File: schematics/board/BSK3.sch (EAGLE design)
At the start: 19 parts

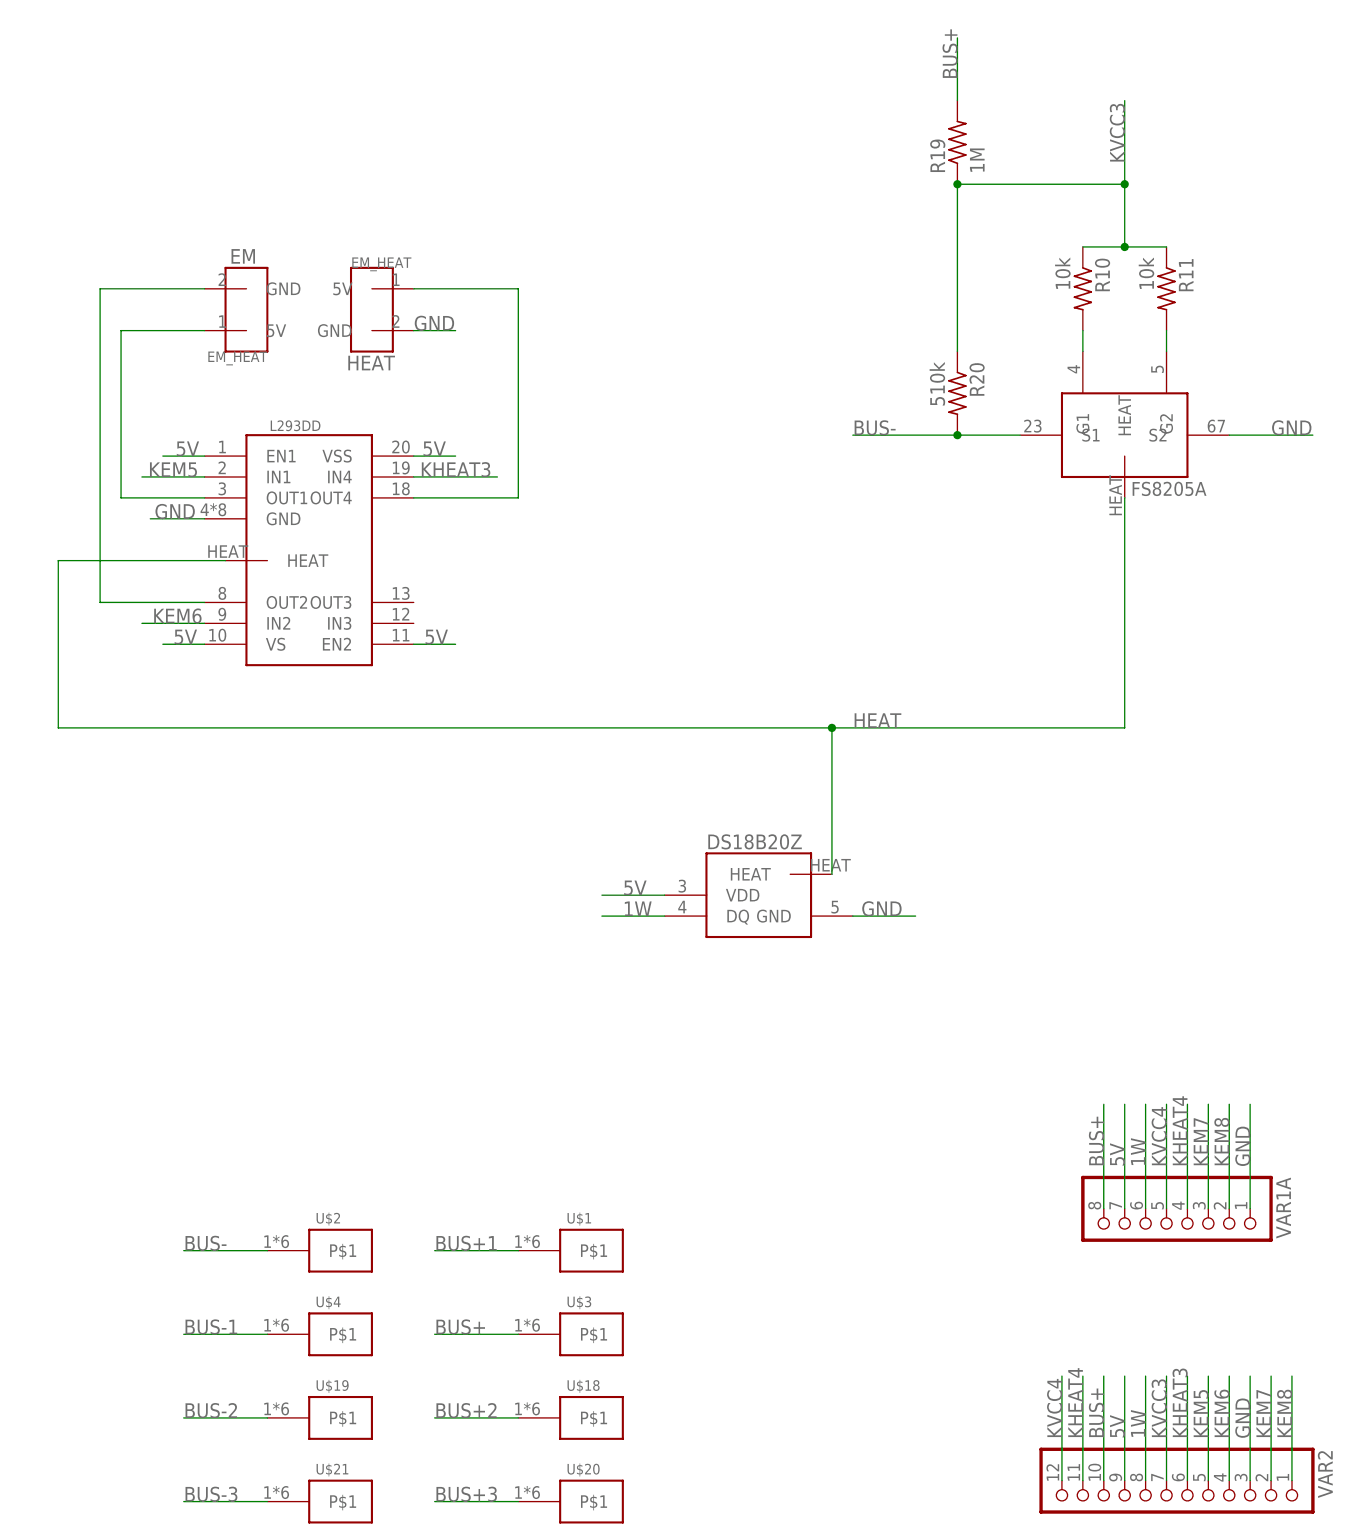
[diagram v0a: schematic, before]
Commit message: Реструктурированы сигналы коммутации для плат БСК
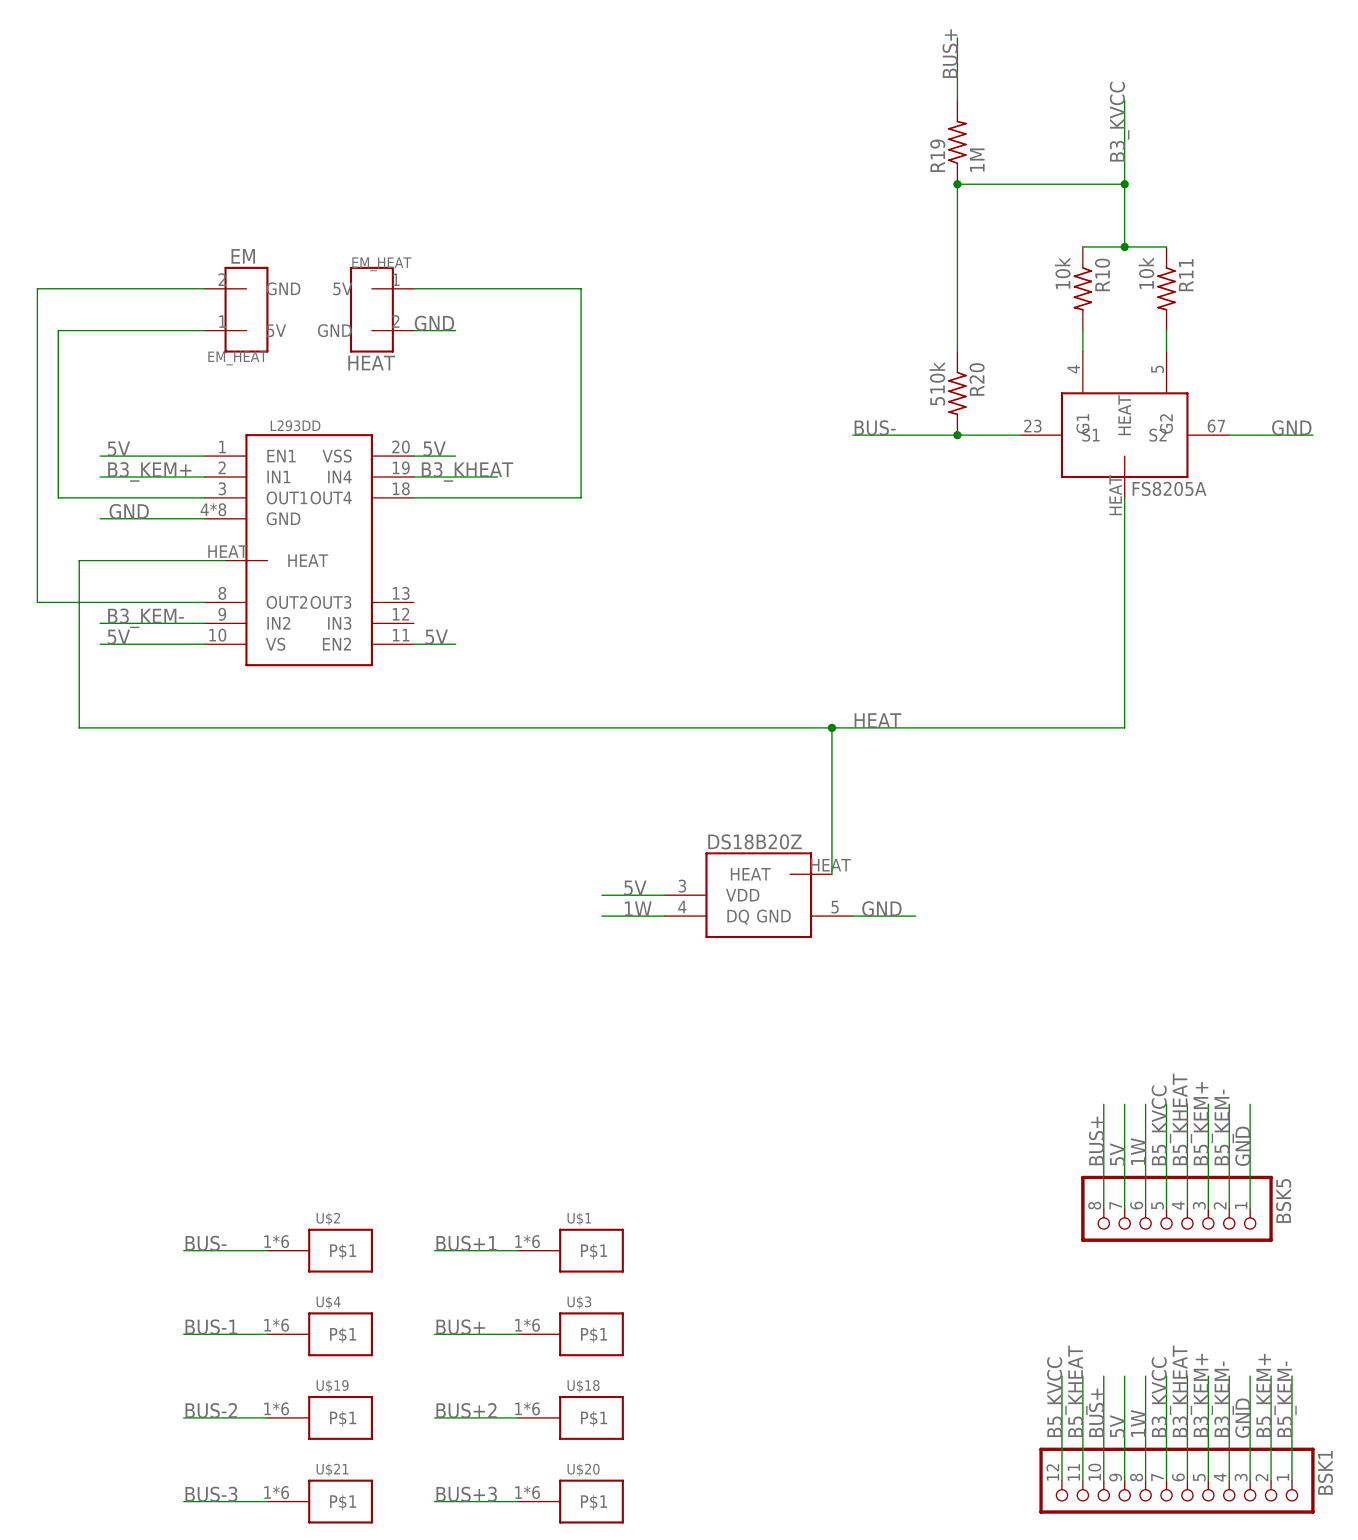
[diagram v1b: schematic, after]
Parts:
- renumbered VAR1A to BSK5, VAR2 to BSK1
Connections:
- net KEM5 renamed B3_KEM+
- net KEM6 renamed B3_KEM-
- net KEM7 renamed B5_KEM+
- net KEM8 renamed B5_KEM-
- net KHEAT3 renamed B3_KHEAT
- net KHEAT4 renamed B5_KHEAT
- net KVCC3 renamed B3_KVCC
- net KVCC4 renamed B5_KVCC

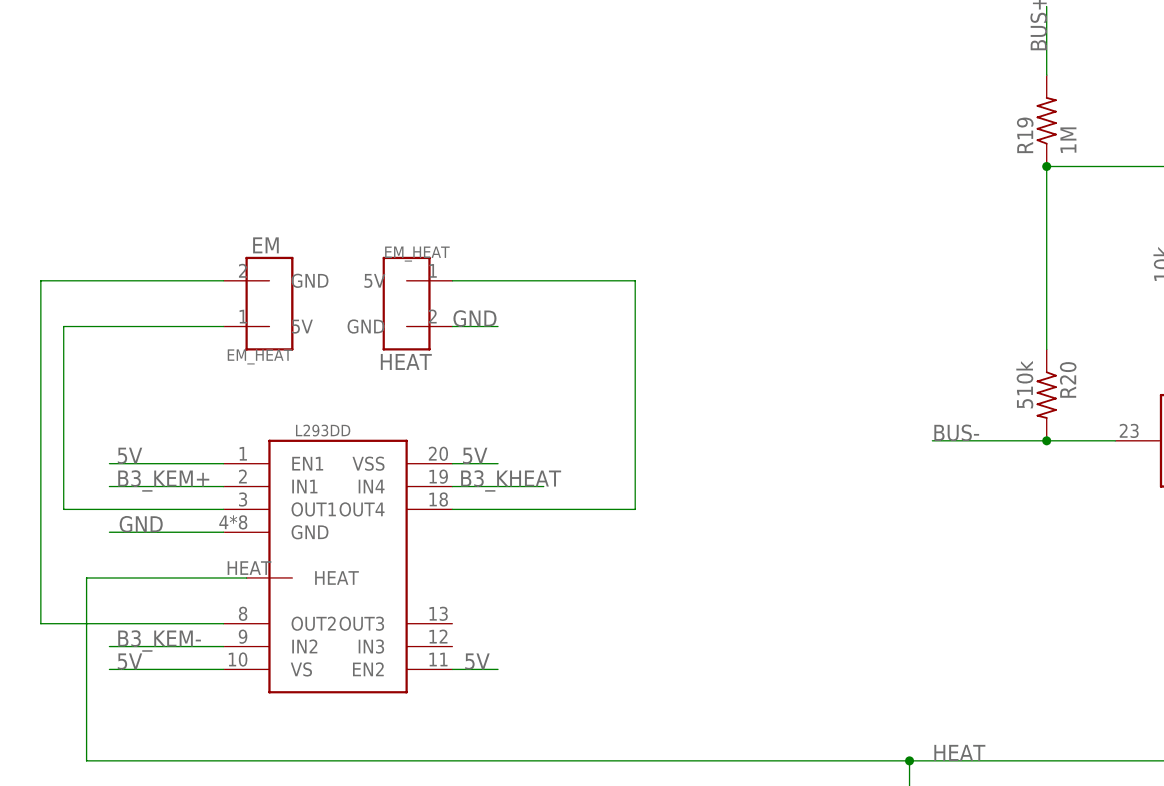
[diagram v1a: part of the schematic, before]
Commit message: Добавлены светодиоды на платы БСК
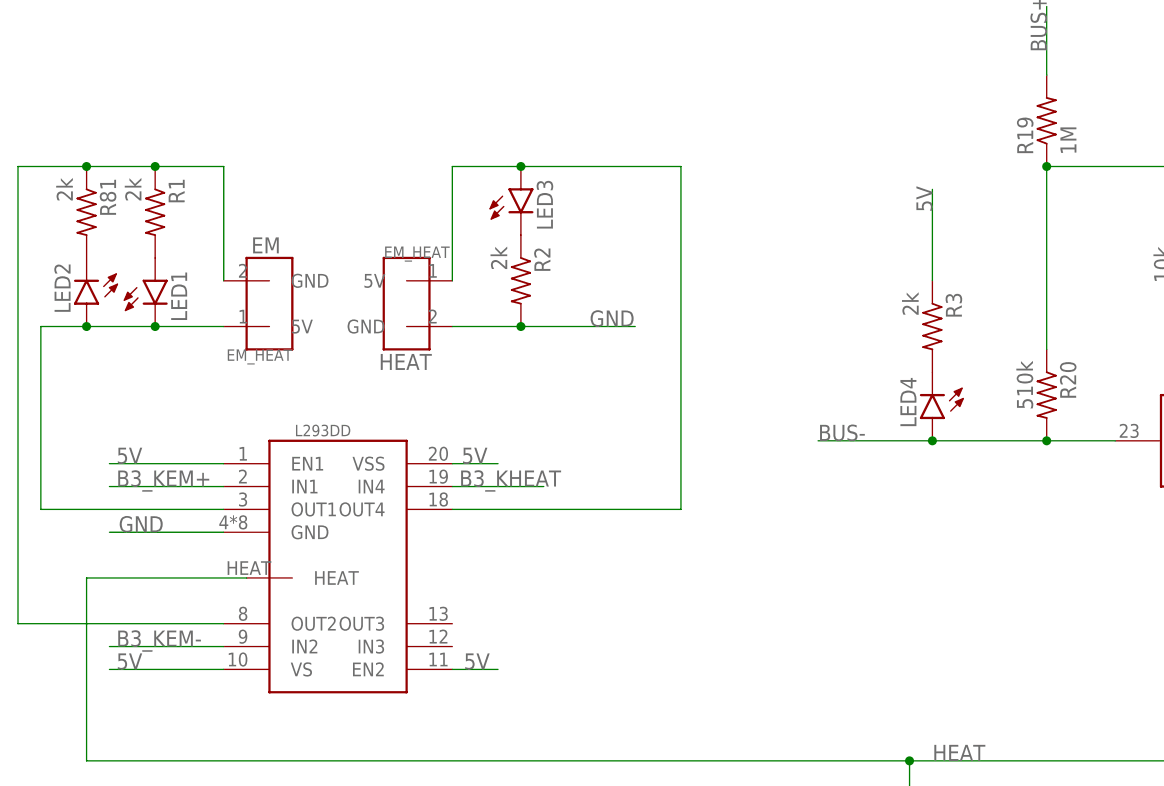
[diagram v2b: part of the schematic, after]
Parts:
- added LED1, LED2, LED3, LED4: (no value), led:LEDCHIPLED_0603
- added R1, R2, R3, R81: 2k, resistor:R-US_R0603
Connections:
- new net N$4: LED2.C, R81.2
- new net N$5: LED1.A, R1.2
- new net N$6: LED3.C, R2.1
- new net N$7: LED4.C, R3.2
- net 5V: now also R3.1
- net BUS-: now also LED4.A
- net GND: now also R2.2
- net N$1: now also LED1.C, LED2.A
- net N$2: now also R1.1, R81.1
- net N$3: now also LED3.A
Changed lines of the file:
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@@
 <part name="U$21" library="CanCubeSat" deviceset="KCONNECT" device=""/>
 <part name="BSK5" library="pinheadCS" deviceset="PINHD-1X8" device=""/>
+<part name="LED2" library="led" library_urn="urn:adsk.eagle:library:259" deviceset="LED" device="CHIPLED_0603" package3d_urn="urn:adsk.eagle:package:15822/2"/>
+<part name="R81" library="resistor" library_urn="urn:adsk.eagle:library:348" deviceset="R-US_" device="R0603" package3d_urn="urn:adsk.eagle:package:23555/3" value="2k"/>
+<part name="R1" library="resistor" library_urn="urn:adsk.eagle:library:348" deviceset="R-US_" device="R0603" package3d_urn="urn:adsk.eagle:package:23555/3" value="2k"/>
+<part name="LED1" library="led" library_urn="urn:adsk.eagle:library:259" deviceset="LED" device="CHIPLED_0603" package3d_urn="urn:adsk.eagle:package:15822/2"/>
+<part name="R2" library="resistor" library_urn="urn:adsk.eagle:library:348" deviceset="R-US_" device="R0603" package3d_urn="urn:adsk.eagle:package:23555/3" value="2k"/>
+<part name="LED3" library="led" library_urn="urn:adsk.eagle:library:259" deviceset="LED" device="CHIPLED_0603" package3d_urn="urn:adsk.eagle:package:15822/2"/>
+<part name="LED4" library="led" library_urn="urn:adsk.eagle:library:259" deviceset="LED" device="CHIPLED_0603" package3d_urn="urn:adsk.eagle:package:15822/2"/>
+<part name="R3" library="resistor" library_urn="urn:adsk.eagle:library:348" deviceset="R-US_" device="R0603" package3d_urn="urn:adsk.eagle:package:23555/3" value="2k"/>
 </parts>
 <sheets>
@@
 <attribute name="VALUE" x="154.94" y="125.73" size="1.778" layer="96" rot="R270"/>
 </instance>
+<instance part="LED2" gate="G$1" x="35.56" y="231.14" smashed="yes" rot="R180">
+<attribute name="NAME" x="32.004" y="235.712" size="1.778" layer="95" rot="R270"/>
+<attribute name="VALUE" x="29.845" y="235.712" size="1.778" layer="96" rot="R270"/>
+</instance>
+<instance part="R81" gate="G$1" x="35.56" y="241.3" smashed="yes" rot="R270">
+<attribute name="NAME" x="37.0586" y="245.11" size="1.778" layer="95" rot="R270"/>
+<attribute name="VALUE" x="32.258" y="245.11" size="1.778" layer="96" rot="R270"/>
+</instance>
+<instance part="R1" gate="G$1" x="43.18" y="241.3" smashed="yes" rot="R270">
+<attribute name="NAME" x="44.6786" y="245.11" size="1.778" layer="95" rot="R270"/>
+<attribute name="VALUE" x="39.878" y="245.11" size="1.778" layer="96" rot="R270"/>
+</instance>
+<instance part="LED1" gate="G$1" x="43.18" y="233.68" smashed="yes">
+<attribute name="NAME" x="46.736" y="229.108" size="1.778" layer="95" rot="R90"/>
+<attribute name="VALUE" x="48.895" y="229.108" size="1.778" layer="96" rot="R90"/>
+</instance>
+<instance part="R2" gate="G$1" x="83.82" y="233.68" smashed="yes" rot="R270">
+<attribute name="NAME" x="85.3186" y="237.49" size="1.778" layer="95" rot="R270"/>
+<attribute name="VALUE" x="80.518" y="237.49" size="1.778" layer="96" rot="R270"/>
+</instance>
+<instance part="LED3" gate="G$1" x="83.82" y="243.84" smashed="yes">
+<attribute name="NAME" x="87.376" y="239.268" size="1.778" layer="95" rot="R90"/>
+<attribute name="VALUE" x="89.535" y="239.268" size="1.778" layer="96" rot="R90"/>
+</instance>
+<instance part="LED4" gate="G$1" x="129.54" y="218.44" smashed="yes" rot="R180">
+<attribute name="NAME" x="125.984" y="223.012" size="1.778" layer="95" rot="R270"/>
+<attribute name="VALUE" x="123.825" y="223.012" size="1.778" layer="96" rot="R270"/>
+</instance>
+<instance part="R3" gate="G$1" x="129.54" y="228.6" smashed="yes" rot="R270">
+<attribute name="NAME" x="131.0386" y="232.41" size="1.778" layer="95" rot="R270"/>
+<attribute name="VALUE" x="126.238" y="232.41" size="1.778" layer="96" rot="R270"/>
+</instance>
 </instances>
 <busses>
@@
 <net name="GND" class="0">
 <segment>
-<wire x1="76.2" y1="228.6" x2="81.28" y2="228.6" width="0.1524" layer="91"/>
-<label x="76.2" y="228.6" size="1.778" layer="95"/>
+<wire x1="76.2" y1="228.6" x2="83.82" y2="228.6" width="0.1524" layer="91"/>
+<label x="91.44" y="228.6" size="1.778" layer="95"/>
 <pinref part="U$7" gate="G$1" pin="GND"/>
+<pinref part="R2" gate="G$1" pin="2"/>
+<wire x1="83.82" y1="228.6" x2="96.52" y2="228.6" width="0.1524" layer="91"/>
+<junction x="83.82" y="228.6"/>
 </segment>
 <segment>
@@
 <label x="101.6" y="160.02" size="1.778" layer="95"/>
 </segment>
+<segment>
+<wire x1="129.54" y1="233.68" x2="129.54" y2="243.84" width="0.1524" layer="91"/>
+<pinref part="R3" gate="G$1" pin="1"/>
+<label x="129.54" y="241.3" size="1.778" layer="95" rot="R90"/>
+</segment>
 </net>
 <net name="1W" class="0">
@@
 <segment>
 <pinref part="U$6" gate="G$1" pin="5V"/>
-<wire x1="50.8" y1="228.6" x2="33.02" y2="228.6" width="0.1524" layer="91"/>
-<wire x1="33.02" y1="228.6" x2="33.02" y2="208.28" width="0.1524" layer="91"/>
+<wire x1="50.8" y1="228.6" x2="43.18" y2="228.6" width="0.1524" layer="91"/>
+<wire x1="43.18" y1="228.6" x2="35.56" y2="228.6" width="0.1524" layer="91"/>
+<wire x1="35.56" y1="228.6" x2="30.48" y2="228.6" width="0.1524" layer="91"/>
+<wire x1="30.48" y1="228.6" x2="30.48" y2="208.28" width="0.1524" layer="91"/>
 <pinref part="U$8" gate="G$1" pin="OUT1"/>
-<wire x1="33.02" y1="208.28" x2="50.8" y2="208.28" width="0.1524" layer="91"/>
+<wire x1="30.48" y1="208.28" x2="50.8" y2="208.28" width="0.1524" layer="91"/>
+<pinref part="LED2" gate="G$1" pin="A"/>
+<junction x="35.56" y="228.6"/>
+<pinref part="LED1" gate="G$1" pin="C"/>
+<junction x="43.18" y="228.6"/>
 </segment>
 </net>
 <net name="N$2" class="0">
 <segment>
+<wire x1="27.94" y1="246.38" x2="27.94" y2="195.58" width="0.1524" layer="91"/>
+<pinref part="U$8" gate="G$1" pin="OUT2"/>
+<wire x1="27.94" y1="195.58" x2="50.8" y2="195.58" width="0.1524" layer="91"/>
 <pinref part="U$6" gate="G$1" pin="GND"/>
-<wire x1="50.8" y1="233.68" x2="30.48" y2="233.68" width="0.1524" layer="91"/>
-<wire x1="30.48" y1="233.68" x2="30.48" y2="195.58" width="0.1524" layer="91"/>
-<pinref part="U$8" gate="G$1" pin="OUT2"/>
-<wire x1="30.48" y1="195.58" x2="50.8" y2="195.58" width="0.1524" layer="91"/>
+<wire x1="50.8" y1="233.68" x2="50.8" y2="246.38" width="0.1524" layer="91"/>
+<wire x1="50.8" y1="246.38" x2="43.18" y2="246.38" width="0.1524" layer="91"/>
+<pinref part="R81" gate="G$1" pin="1"/>
+<wire x1="43.18" y1="246.38" x2="35.56" y2="246.38" width="0.1524" layer="91"/>
+<wire x1="35.56" y1="246.38" x2="27.94" y2="246.38" width="0.1524" layer="91"/>
+<junction x="35.56" y="246.38"/>
+<pinref part="R1" gate="G$1" pin="1"/>
+<junction x="43.18" y="246.38"/>
 </segment>
 </net>
 <net name="N$3" class="0">
 <segment>
+<wire x1="101.6" y1="246.38" x2="101.6" y2="208.28" width="0.1524" layer="91"/>
+<pinref part="U$8" gate="G$1" pin="OUT4"/>
+<wire x1="101.6" y1="208.28" x2="76.2" y2="208.28" width="0.1524" layer="91"/>
 <pinref part="U$7" gate="G$1" pin="5V"/>
-<wire x1="76.2" y1="233.68" x2="96.52" y2="233.68" width="0.1524" layer="91"/>
-<wire x1="96.52" y1="233.68" x2="96.52" y2="208.28" width="0.1524" layer="91"/>
-<pinref part="U$8" gate="G$1" pin="OUT4"/>
-<wire x1="96.52" y1="208.28" x2="76.2" y2="208.28" width="0.1524" layer="91"/>
+<wire x1="76.2" y1="233.68" x2="76.2" y2="246.38" width="0.1524" layer="91"/>
+<wire x1="76.2" y1="246.38" x2="83.82" y2="246.38" width="0.1524" layer="91"/>
+<pinref part="LED3" gate="G$1" pin="A"/>
+<wire x1="83.82" y1="246.38" x2="101.6" y2="246.38" width="0.1524" layer="91"/>
+<junction x="83.82" y="246.38"/>
 </segment>
 </net>
@@
 <wire x1="142.24" y1="215.9" x2="129.54" y2="215.9" width="0.1524" layer="91"/>
 <junction x="142.24" y="215.9"/>
-<label x="129.54" y="215.9" size="1.778" layer="95"/>
+<label x="116.84" y="215.9" size="1.778" layer="95"/>
+<pinref part="LED4" gate="G$1" pin="A"/>
+<wire x1="129.54" y1="215.9" x2="116.84" y2="215.9" width="0.1524" layer="91"/>
+<junction x="129.54" y="215.9"/>
 </segment>
 <segment>
@@
 </segment>
 </net>
+<net name="N$4" class="0">
+<segment>
+<pinref part="R81" gate="G$1" pin="2"/>
+<pinref part="LED2" gate="G$1" pin="C"/>
+</segment>
+</net>
+<net name="N$5" class="0">
+<segment>
+<pinref part="LED1" gate="G$1" pin="A"/>
+<pinref part="R1" gate="G$1" pin="2"/>
+</segment>
+</net>
+<net name="N$6" class="0">
+<segment>
+<pinref part="LED3" gate="G$1" pin="C"/>
+<pinref part="R2" gate="G$1" pin="1"/>
+</segment>
+</net>
+<net name="N$7" class="0">
+<segment>
+<pinref part="R3" gate="G$1" pin="2"/>
+<pinref part="LED4" gate="G$1" pin="C"/>
+</segment>
+</net>
